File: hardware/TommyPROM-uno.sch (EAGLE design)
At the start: 7 parts, among them IC1 74LS164N, IC2 74LS164N, IC3 AT28C256

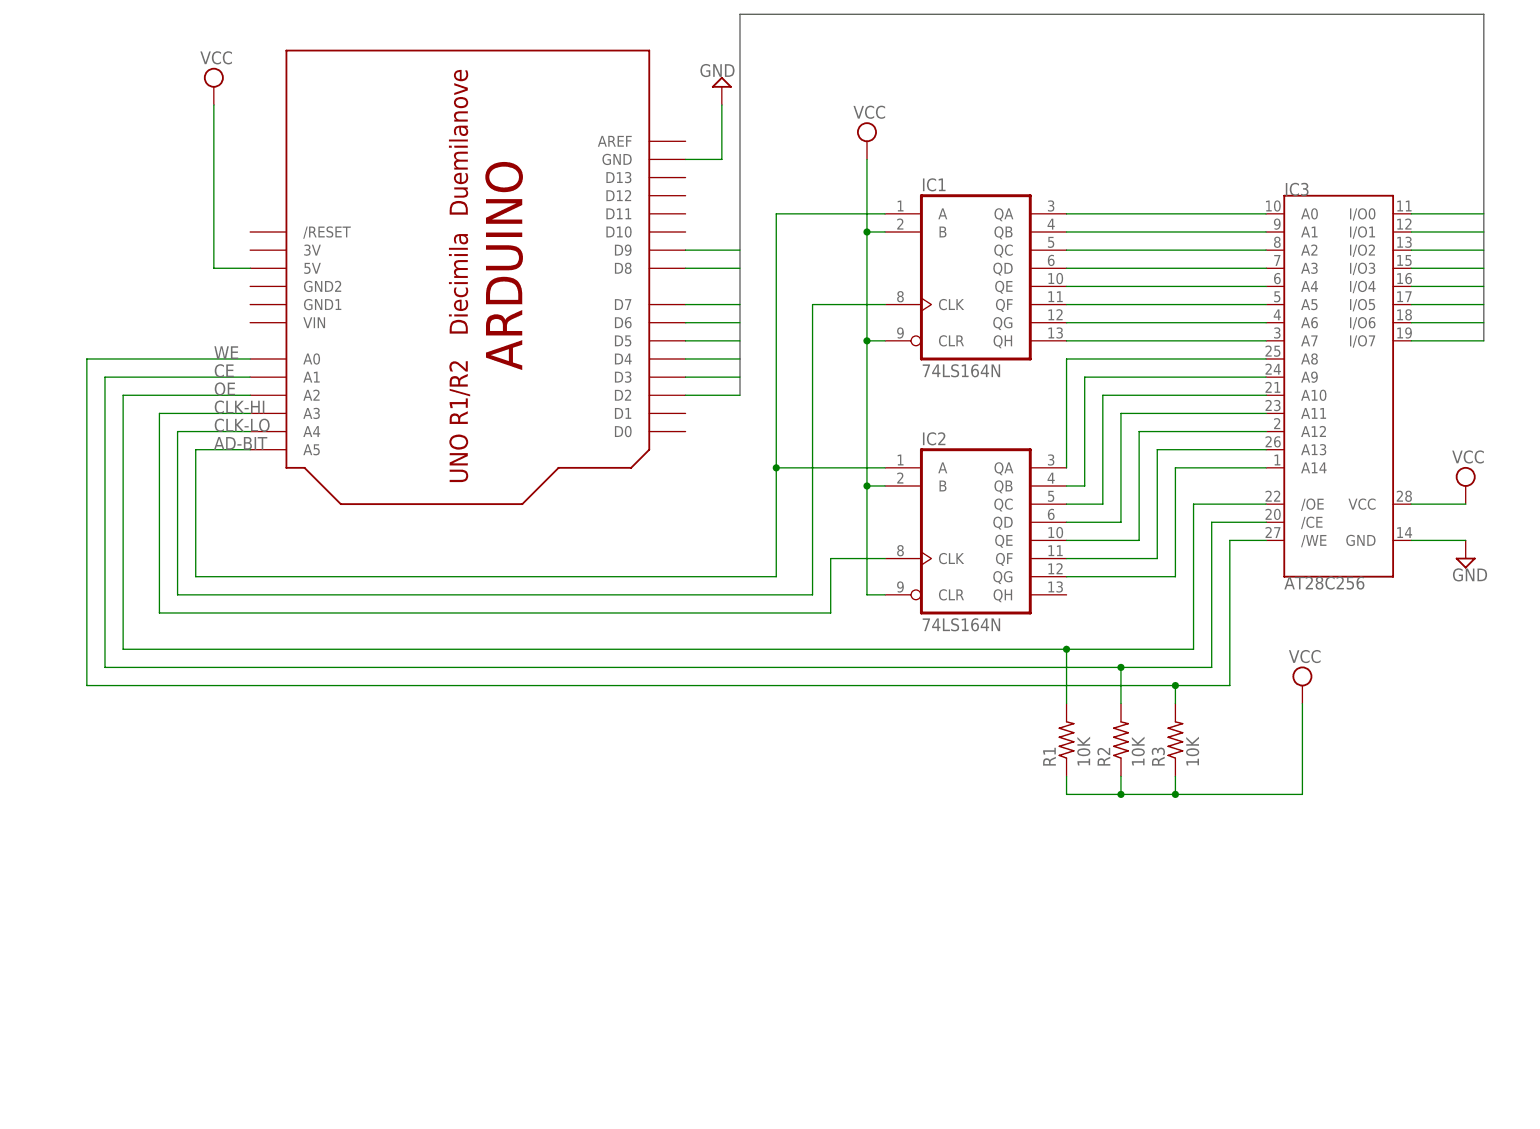
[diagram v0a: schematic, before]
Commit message: Modifications to use 74HC595 shift registers instead of the original 74LS164
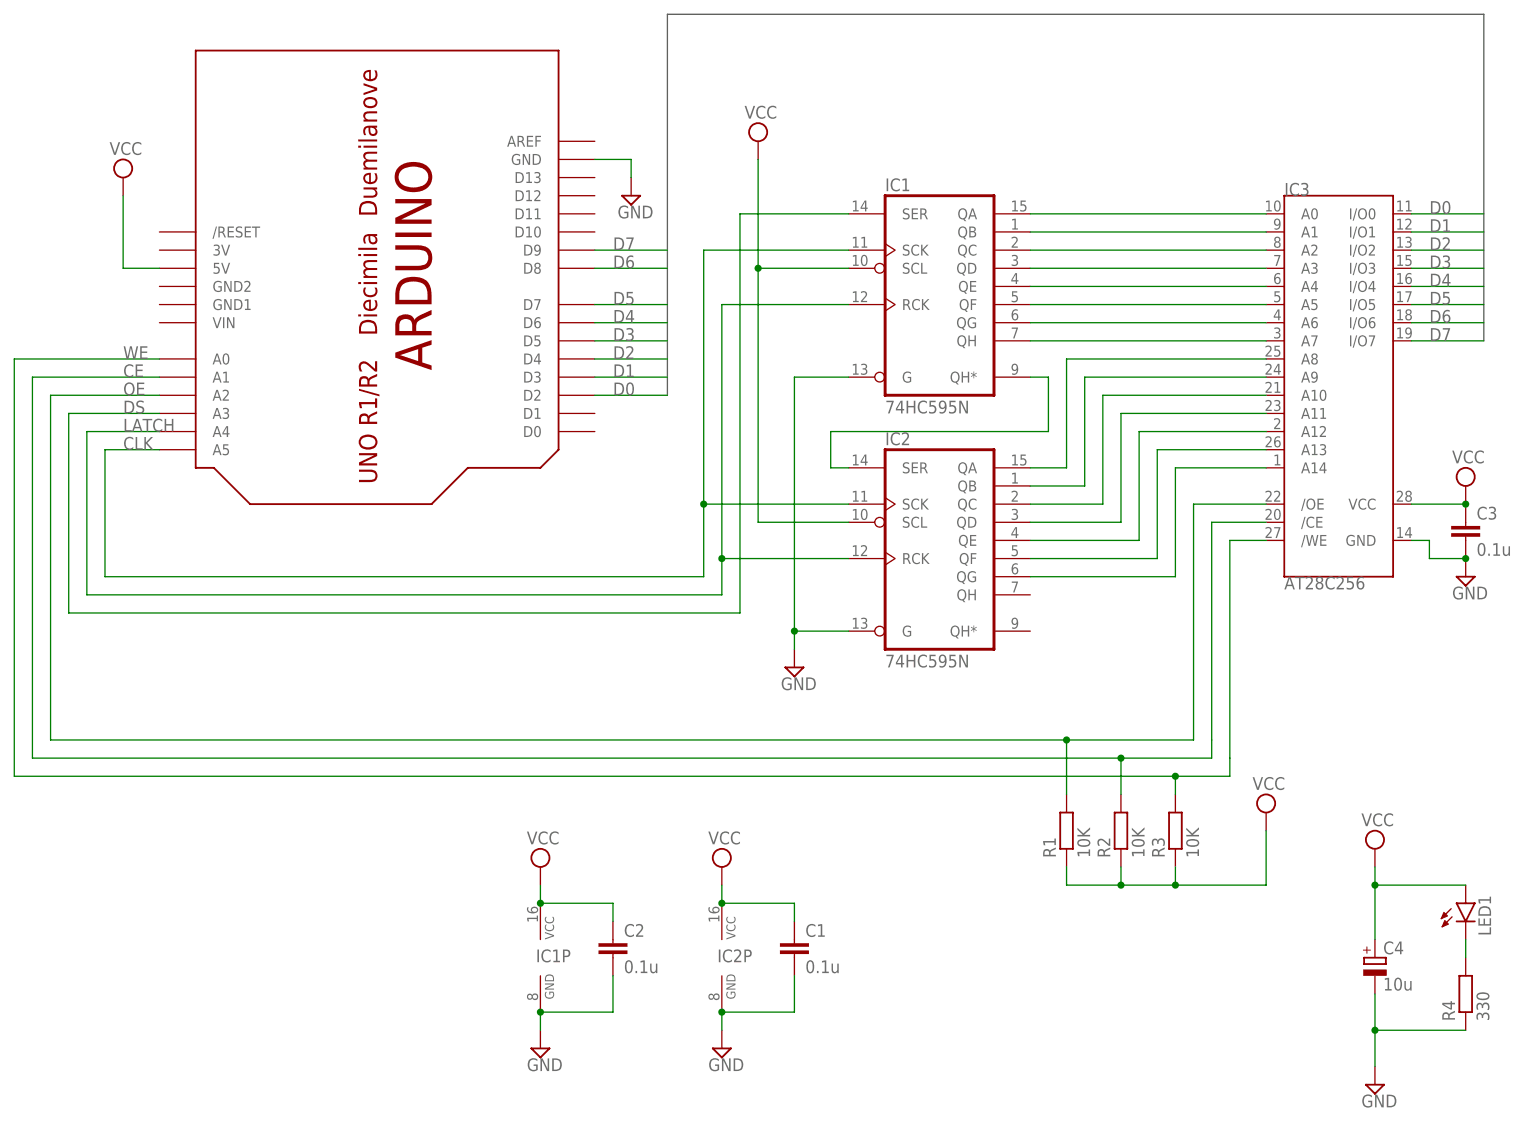
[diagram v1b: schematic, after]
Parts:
- added C1, C2, C3: 0.1u, rcl:C-EU025-025X050
- added C4: 10u, rcl:CPOL-EUE2-5
- added LED1: (no value), led:LED5MM
- added R4: 330, rcl:R-EU_0204/7
- IC1, IC2: value 74LS164N -> 74HC595N; device 74xx-us:74LS164N -> 74xx-eu:74HC595N
- R1, R2, R3: device resistor:R-US_0204/5 -> rcl:R-EU_0204/7
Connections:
- removed net AD-BIT: IC1A.A, IC2A.A, U$1.A5
- removed net CLK-HI: IC2A.CLK, U$1.A3
- removed net CLK-LO: IC1A.CLK, U$1.A4
- new net CLK: IC1A.SCK, IC2A.SCK, U$1.A5
- new net DS: IC1A.SER, U$1.A3
- new net LATCH: IC1A.RCK, IC2A.RCK, U$1.A4
- new net N$1: IC1A.QH*, IC2A.SER
- new net N$2: LED1.C, R4.2
- net GND: now also C1.2, C2.2, C3.2, C4.-, IC1A.G, IC1P.GND, IC2A.G, IC2P.GND, R4.1
- net VCC: now also C1.1, C2.1, C3.1, C4.+, IC1A.SCL, IC1P.VCC, IC2A.SCL, IC2P.VCC, LED1.A; no longer IC1A.B, IC1A.CLR, IC2A.B, IC2A.CLR
